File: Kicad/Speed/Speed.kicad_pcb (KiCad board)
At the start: 2 copper layers, 210.8 x 105.4 mm, 48 parts, among them IC1 LK112M60TR, IC10 PI3B3251QE, IC2 AP7365-33WG-7, IC3 LD1117S50C, IC4 DS1813R-10+T&R, IC5 74LVC161PW,112, IC6 74LVC04APW,118, IC7 74LVC138APW-Q100J, IC8 74LVC138APW-Q100J, IC9 SN74CBT3257CPWR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

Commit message: Did something to the SNES controller readers boards.
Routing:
- net GND: track 1993.2 -> 2131.8 mm, vias 47 -> 55
- net ~{Select}_{Device}2: track 90.7 -> 94.7 mm
- net 12V: track 217.2 -> 220.4 mm
- net /3.3V: track 392.4 -> 393.8 mm
- net D2: track 326.1 -> 327.1 mm
- net D3: track 330.2 -> 331.2 mm
- net D0: track 333.5 -> 334.2 mm
- net /~{Reset Switch}: track 58.0 -> 57.4 mm
- net D6: track 323.3 -> 323.8 mm
- net D1: track 326.1 -> 326.6 mm

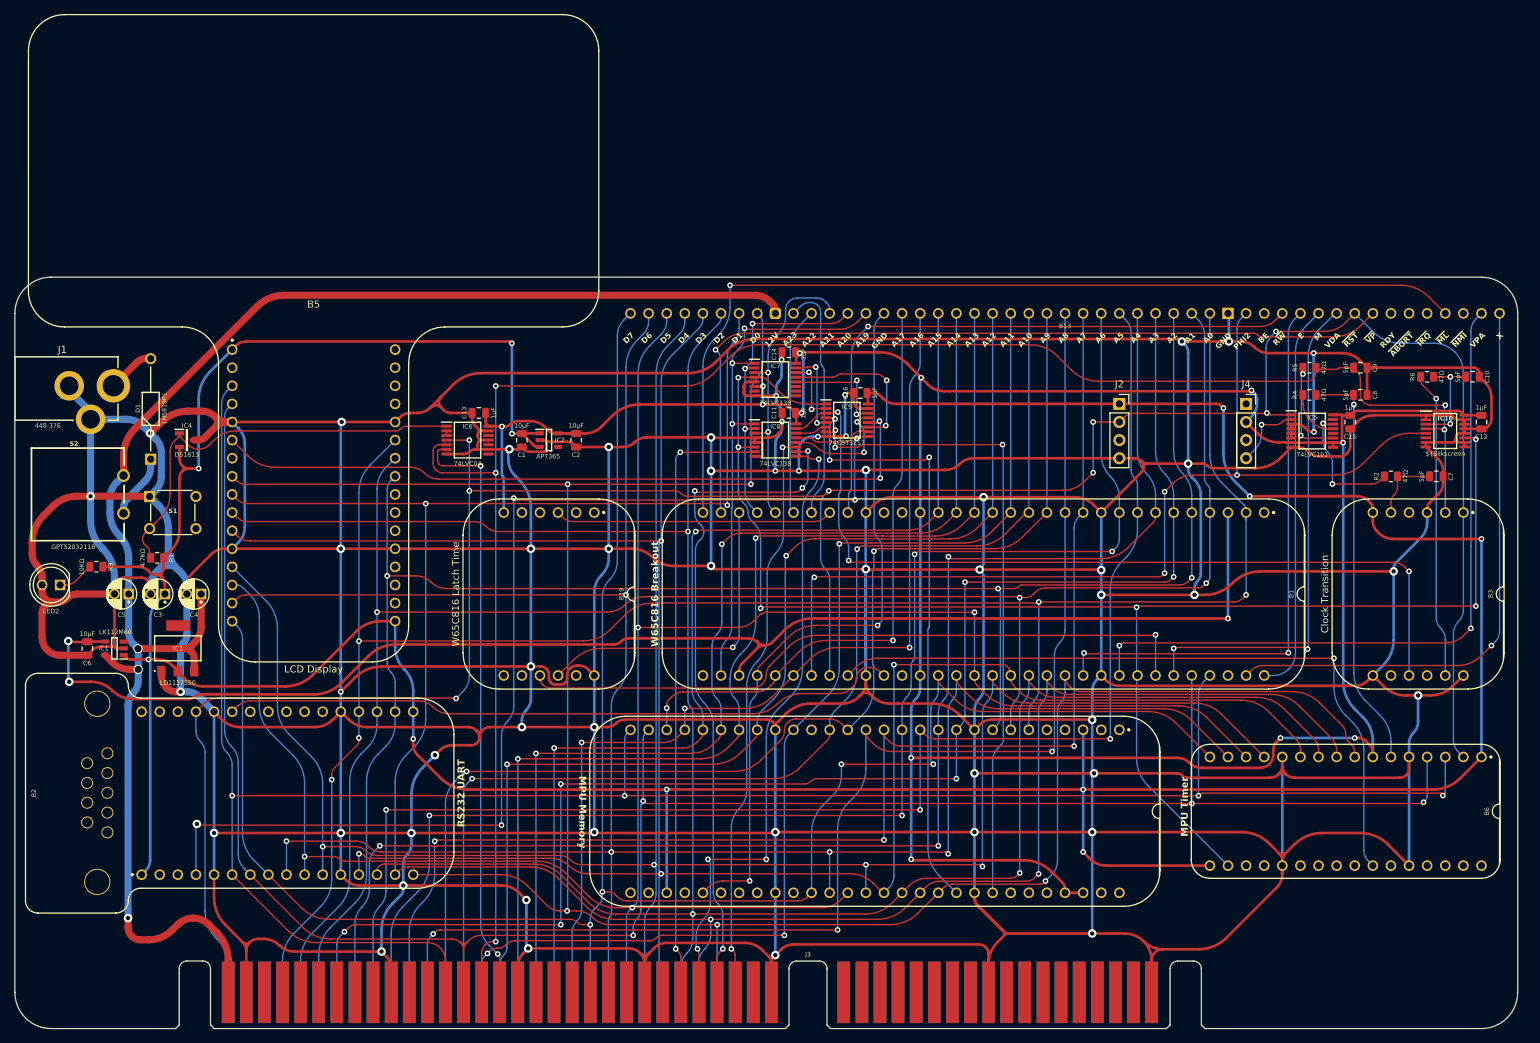
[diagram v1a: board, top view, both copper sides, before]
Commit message: Added more ground to Speed.
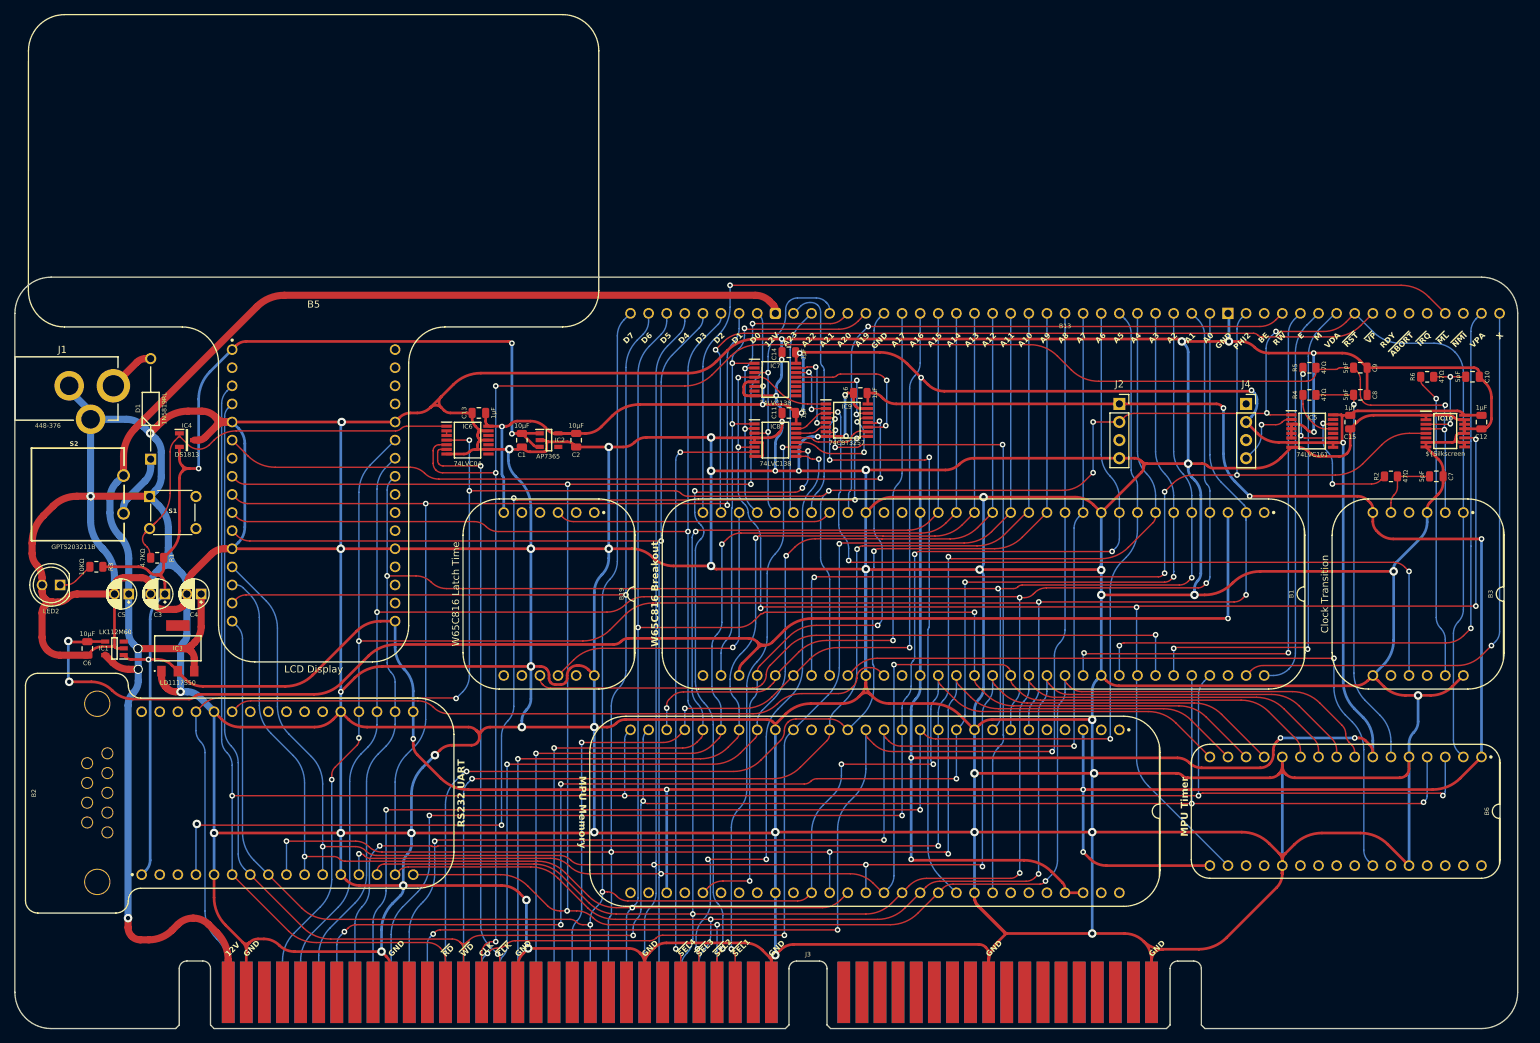
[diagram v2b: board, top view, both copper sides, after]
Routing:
- net GND: track 2131.8 -> 2142.6 mm, vias 55 -> 56
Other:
- board text added: "CLK"
- board text added: "~{CLK}"
- board text added: "~{RD}"
- board text added: "~{Reset}"
- board text added: "~{SEL}1"
- board text added: "~{SEL}2"
- board text added: "~{SEL}3"
- board text added: "~{SEL}4"
- board text added: "~{WD}"

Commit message: Added more ground to Speed.
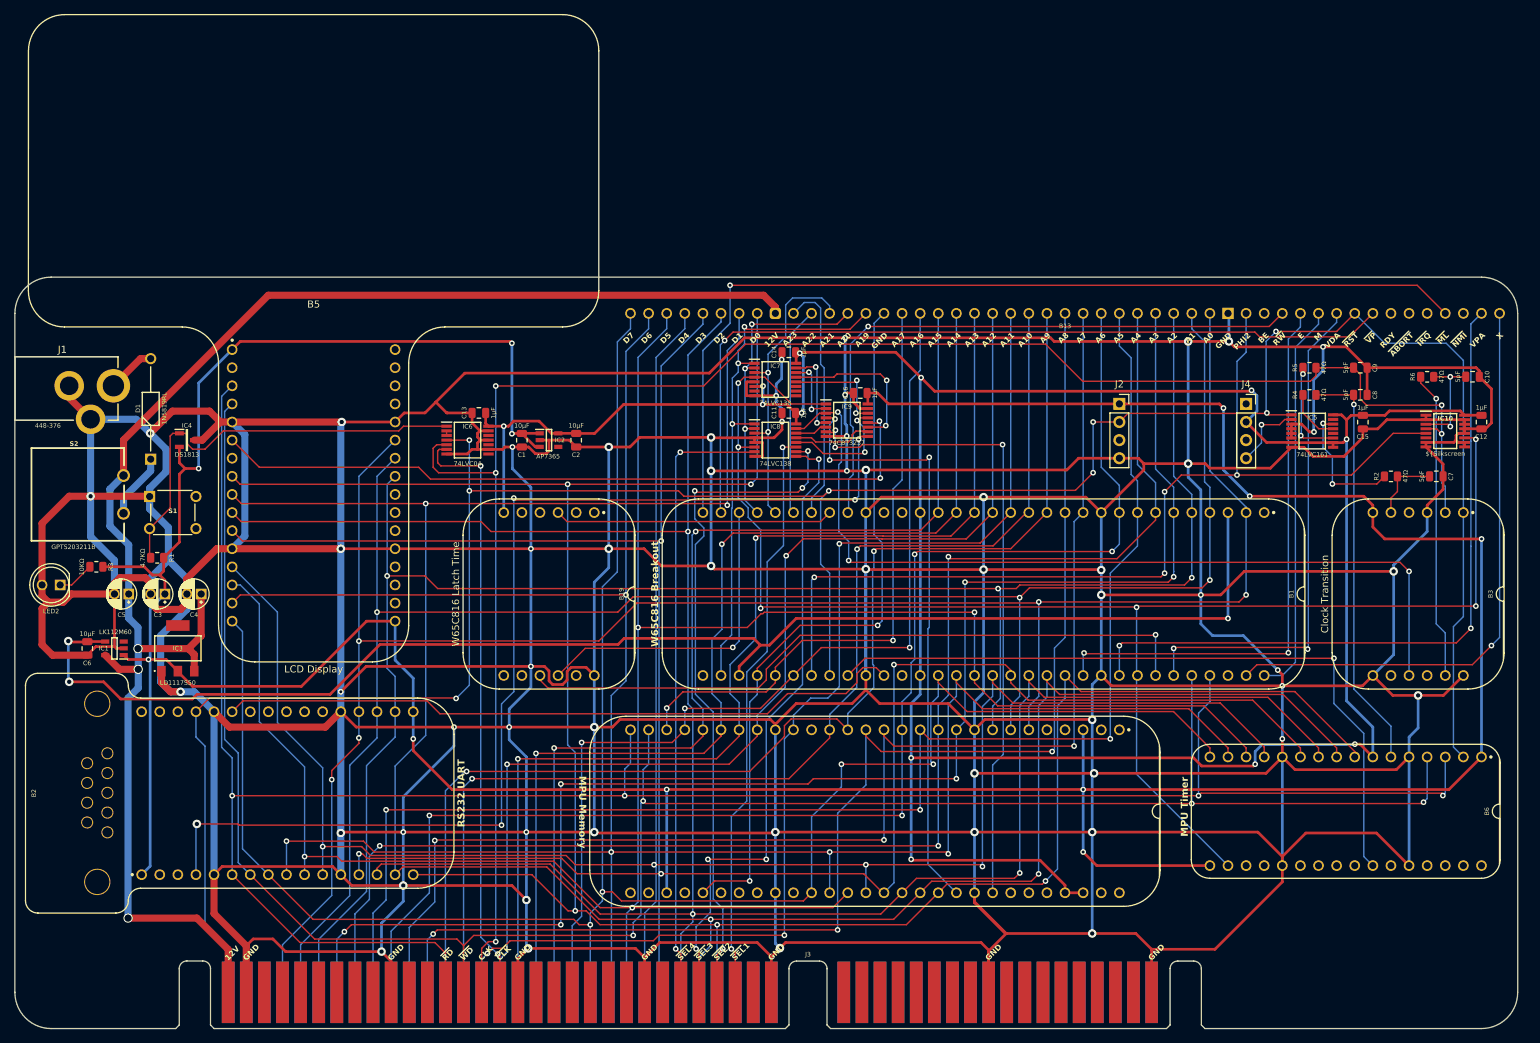
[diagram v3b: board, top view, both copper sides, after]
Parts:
- moved C15 1.78 mm to (222.1, 68.6)
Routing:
- net GND: track 2142.6 -> 2209.6 mm, vias 56 -> 57
- net D2: track 327.1 -> 334.7 mm
- net A11: track 154.4 -> 161.8 mm
- net D1: track 326.6 -> 333.8 mm
- net ~{Reset}: track 361.9 -> 368.8 mm
- net A12: track 149.9 -> 155.6 mm
- net D5: track 319.3 -> 324.1 mm
- net /3.3V: track 393.8 -> 398.2 mm
- net D7: track 299.3 -> 303.5 mm
- net D4: track 311.5 -> 315.5 mm
- net D0: track 334.2 -> 337.3 mm
- net A0: track 268.2 -> 271.3 mm
- net 6.25MHZ: track 258.3 -> 261.0 mm
- net /5V: track 549.9 -> 552.5 mm
- net D6: track 323.8 -> 326.4 mm
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
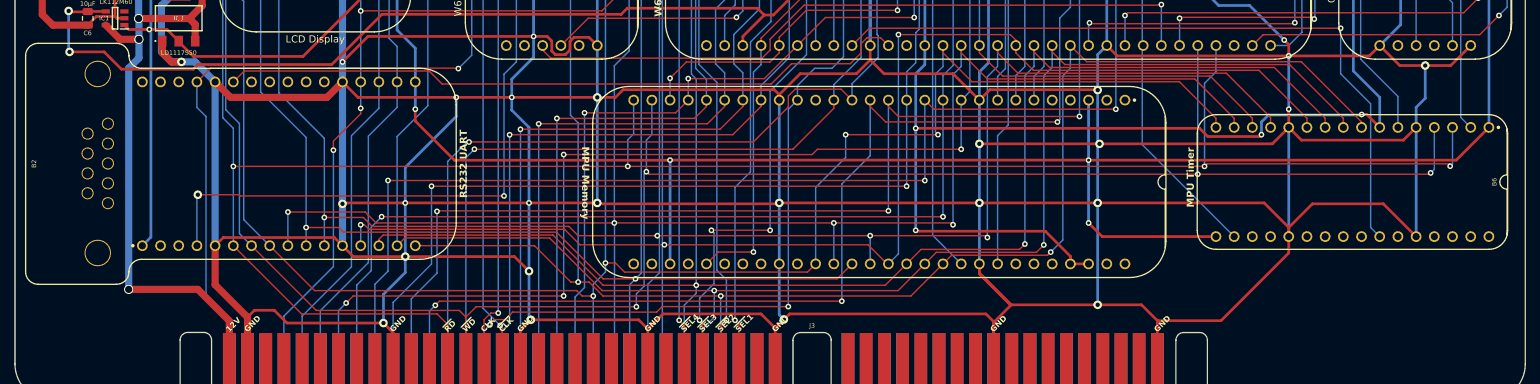
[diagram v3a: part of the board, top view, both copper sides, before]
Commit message: Widened the LCD Display by 2mm.
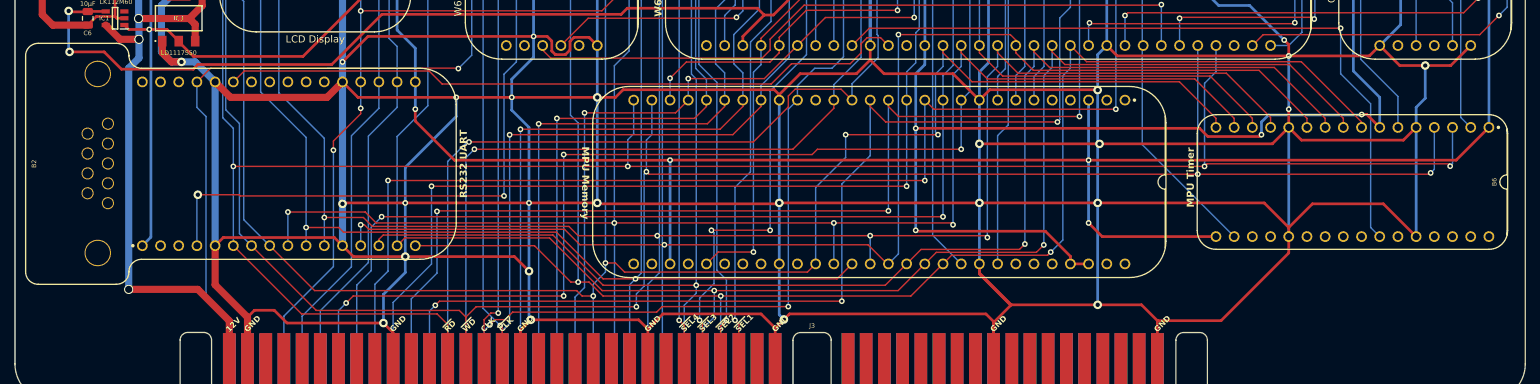
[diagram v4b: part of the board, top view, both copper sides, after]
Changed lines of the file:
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@@
 		(fp_arc
 			(start 26.503803 -16.293381)
-			(mid 27.734591 -15.783562)
+			(mid 27.734626 -15.783568)
 			(end 28.244422 -14.552762)
 			(stroke
@@
 		(fp_arc
 			(start 86.040048 -8.4)
-			(mid 86.357626 -9.156454)
+			(mid 86.35762 -9.156489)
 			(end 87.117096 -9.466799)
 			(stroke
@@
 		(fp_arc
 			(start 90.297 -9.466799)
-			(mid 91.056476 -9.156459)
+			(mid 91.056441 -9.156453)
 			(end 91.374048 -8.4)
 			(stroke
@@
 		(fp_arc
 			(start 139.499048 -8.4)
-			(mid 139.816626 -9.156454)
+			(mid 139.81662 -9.156489)
 			(end 140.576096 -9.466799)
 			(stroke
@@
 		(fp_arc
 			(start 14.404267 -2.613733)
-			(mid 16.252448 -1.848183)
+			(mid 16.252451 -1.848184)
 			(end 17.017999 -0.000001)
 			(stroke
@@
 		(fp_arc
 			(start 24.765028 1.905401)
-			(mid 26.252922 -1.686684)
+			(mid 26.252921 -1.686687)
 			(end 29.845 -3.174599)
 			(stroke

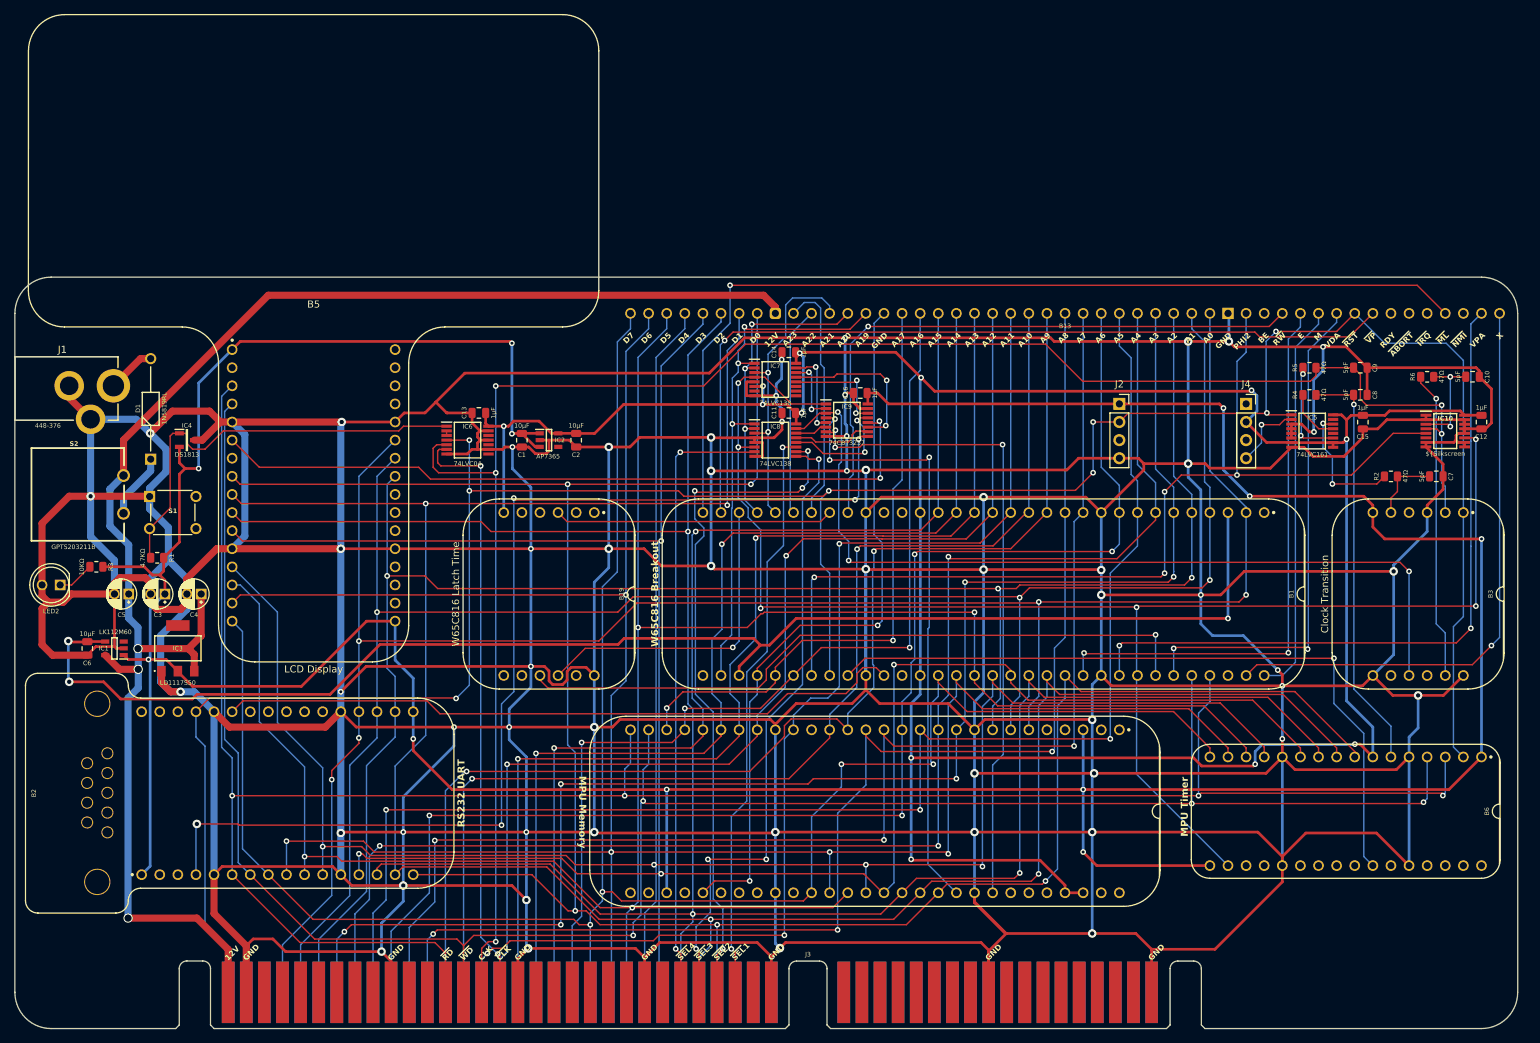
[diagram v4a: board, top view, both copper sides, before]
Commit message: Added a TTL5V UART.
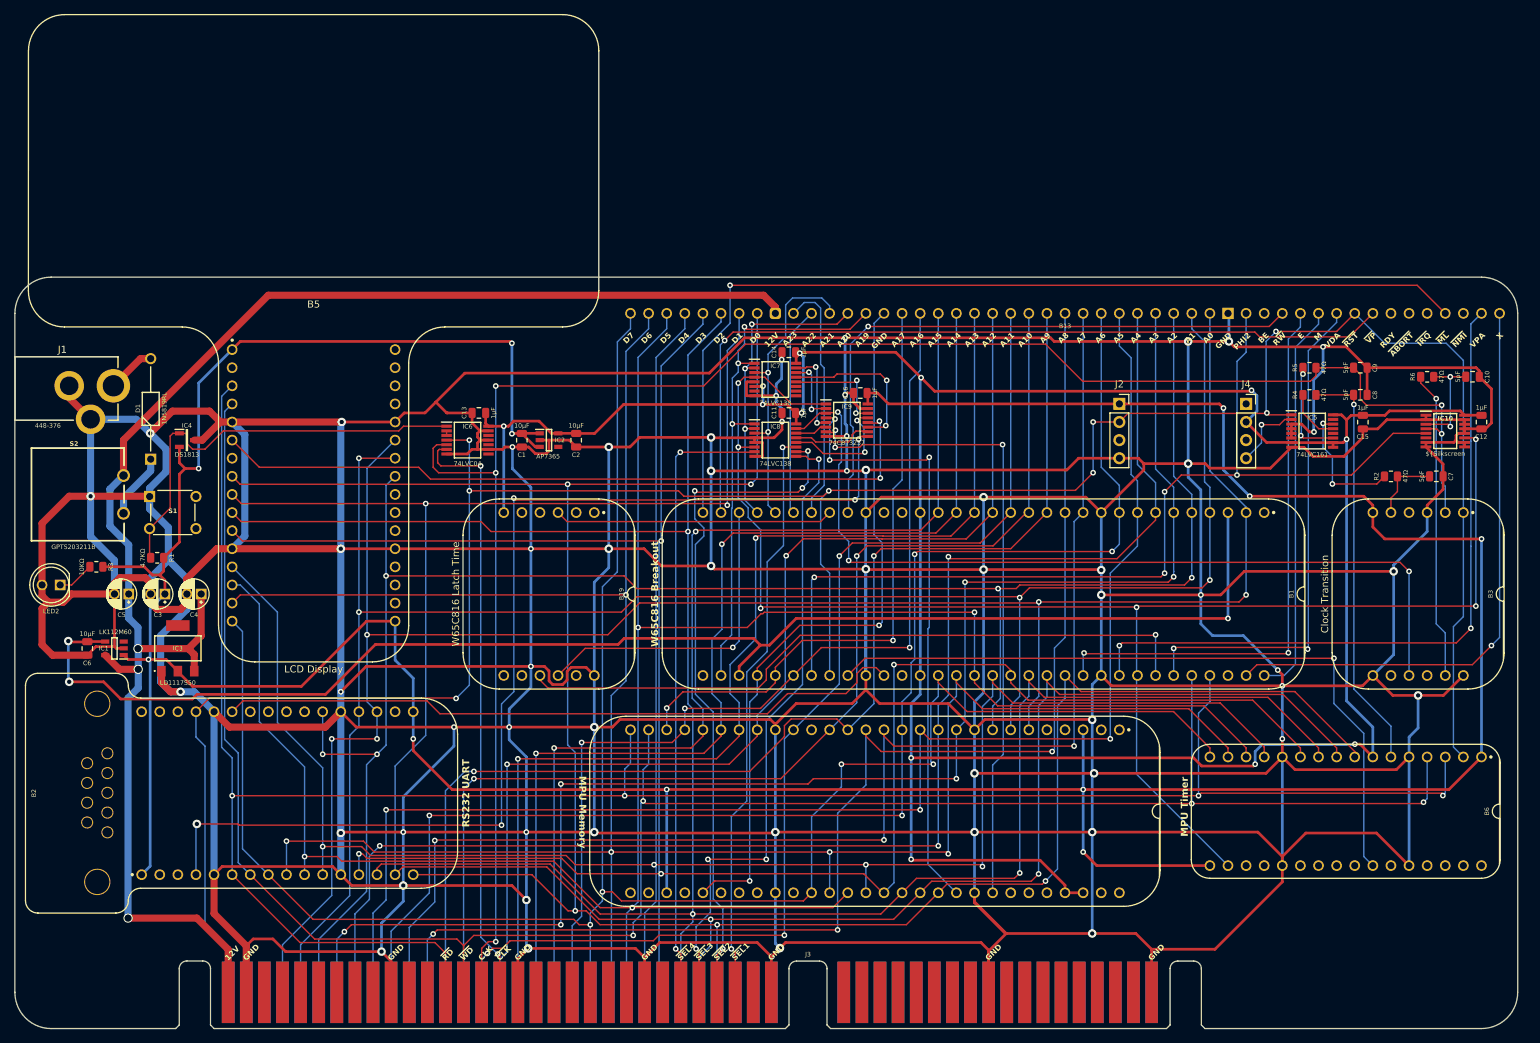
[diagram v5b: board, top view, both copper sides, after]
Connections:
- B2 pad 18: A2 -> unconnected-(B2-1.8432Mhz-Pad18)
- B2 pad 19: A1 -> A0
- B2 pad 20: A0 -> A1
- B2 pad 22: unconnected-(B2-N.C.-Pad22) -> A2
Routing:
- net A2: track 250.5 -> 263.4 mm, vias 3 -> 5
- net A1: track 256.8 -> 262.3 mm, vias 3 -> 4
- net A0: track 271.3 -> 274.6 mm
- net A11: track 161.8 -> 159.4 mm
- net A10: track 164.9 -> 163.6 mm
- net A9: track 171.6 -> 171.1 mm

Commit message: Fixed UART components.
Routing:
- net GND: track 2209.6 -> 2210.1 mm
